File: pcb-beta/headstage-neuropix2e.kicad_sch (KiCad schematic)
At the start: 4 parts, among them J1 X.FL-R-SMT-1(02)

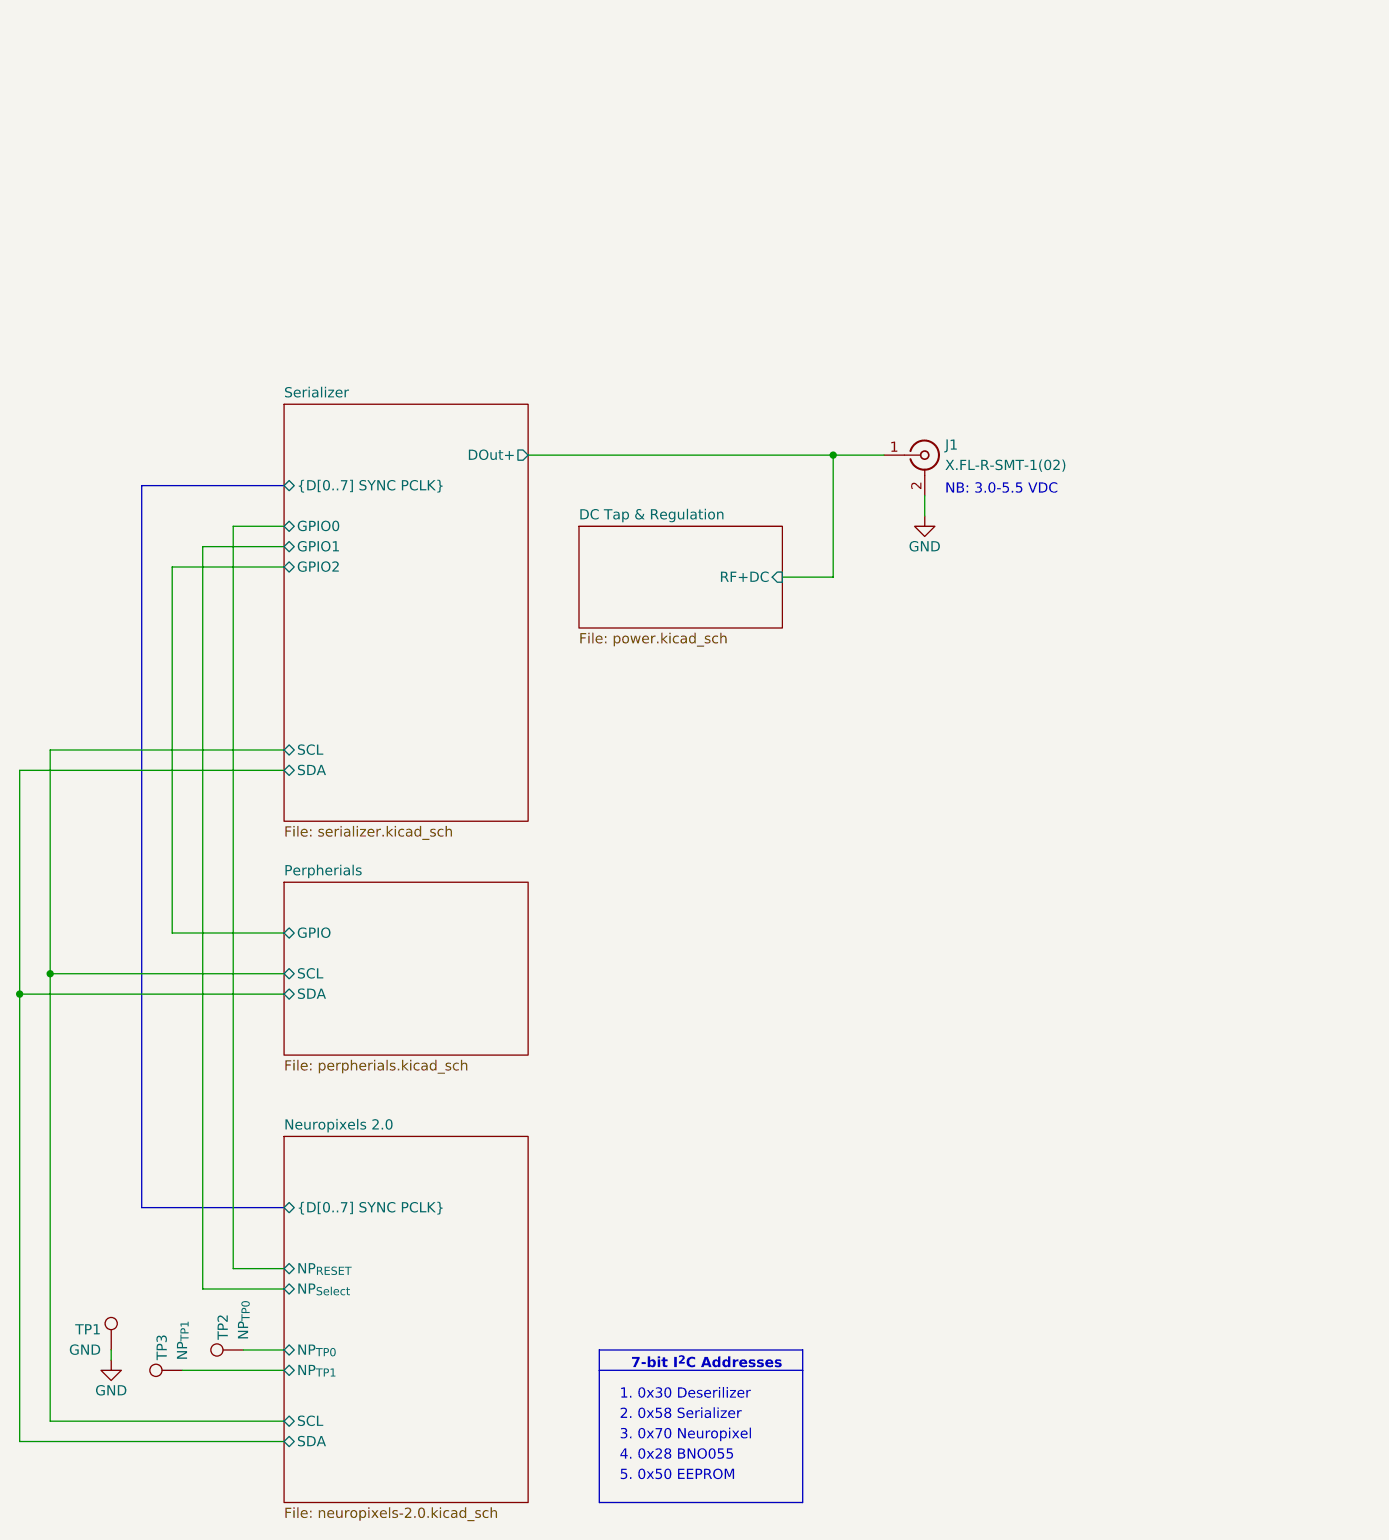
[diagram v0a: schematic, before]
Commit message: Move pcb to pcb-beta directory
- Because this board only works with Beta-test NP2.0 probes
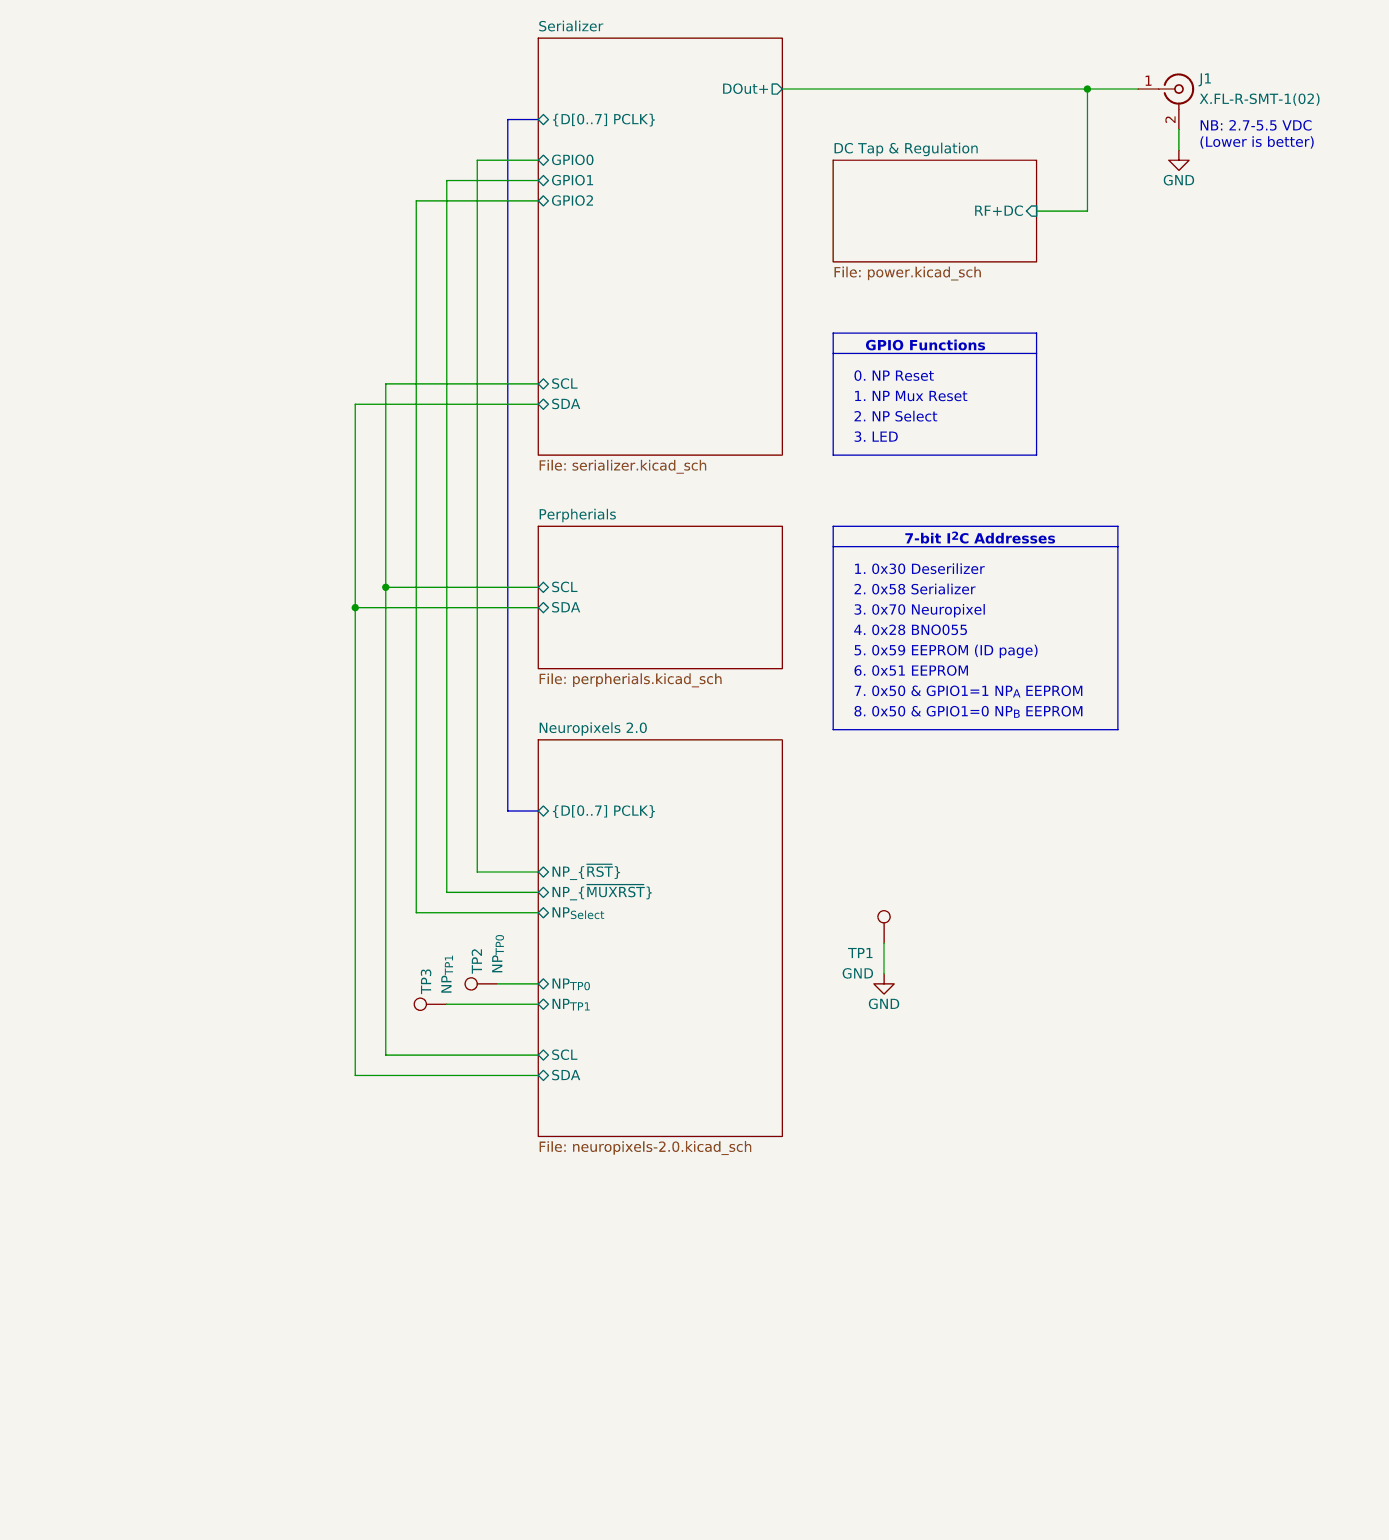
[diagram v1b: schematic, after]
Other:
- sheet Neuropixels 2.0 ports: added NP_{~{MUXRST}}, NP_{~{RST}}, {D[0..7] PCLK}; removed NP_{RESET}, {D[0..7] SYNC PCLK}
- sheet Perpherials ports: added none; removed GPIO
- sheet Serializer ports: added {D[0..7] PCLK}; removed {D[0..7] SYNC PCLK}
- note added: "0. NP Reset"
- note added: "1. NP Mux Reset"
- note added: "2. NP Select"
- note added: "3. LED"
- note added: "5. 0x59 EEPROM (ID page)"
- note added: "6. 0x51 EEPROM"
- note added: "7. 0x50 & GPIO1=1 NP_{A} EEPROM"
- note added: "8. 0x50 & GPIO1=0 NP_{B} EEPROM"
- note added: "GPIO Functions"
- note added: "NB: 2.7-5.5 VDC (Lower is better)"
- note removed: "5. 0x50 EEPROM"
- note removed: "NB: 3.0-5.5 VDC"
- moved on the sheet: J1, TP1, TP2, TP3
